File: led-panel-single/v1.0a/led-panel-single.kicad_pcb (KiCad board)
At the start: 2 copper layers, 40 x 20 mm, 23 parts, among them J1 5V, J2 jmp, J3 HUB75E, J4 PMOD, J5 jmp, U1 SN74LVC8T245, U2 NL27WZ14, U3 CD74HC4024PWR, U4 74VHC574

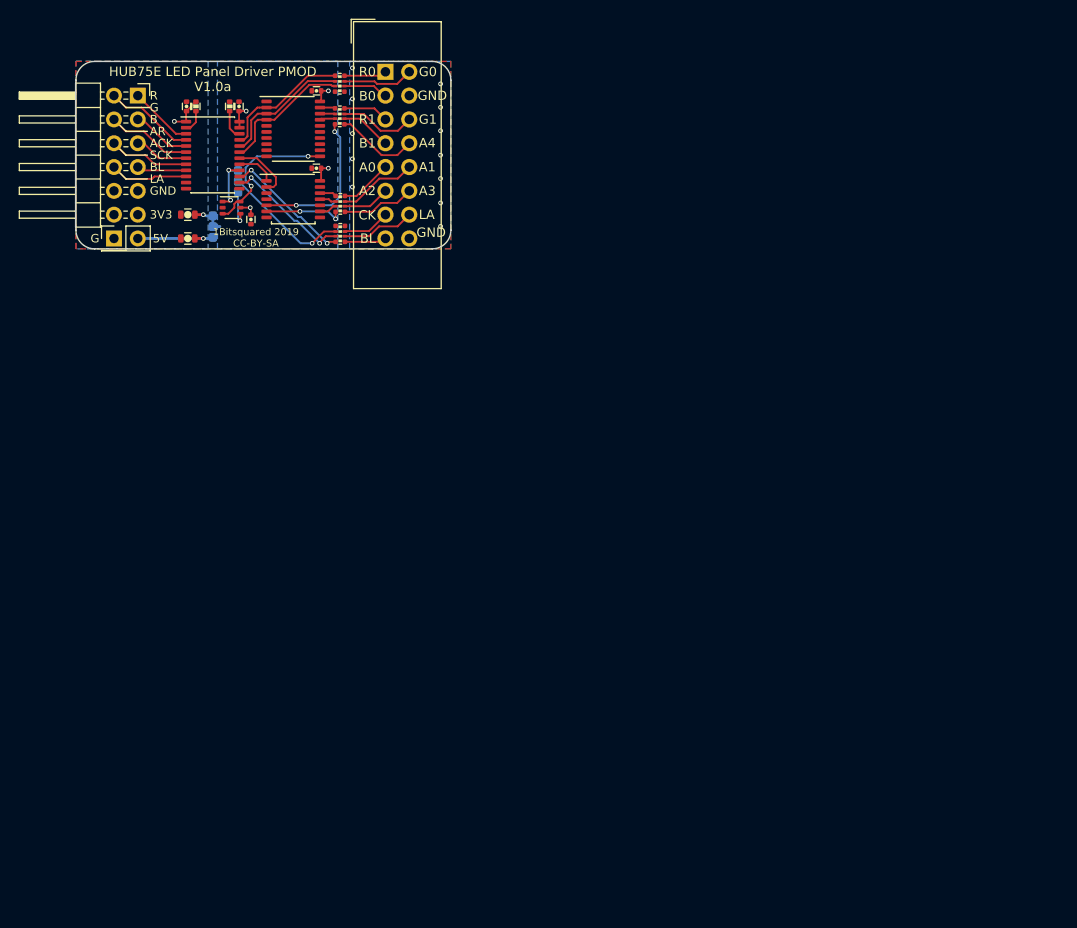
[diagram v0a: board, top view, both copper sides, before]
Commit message: led-panel-single: easy solder version
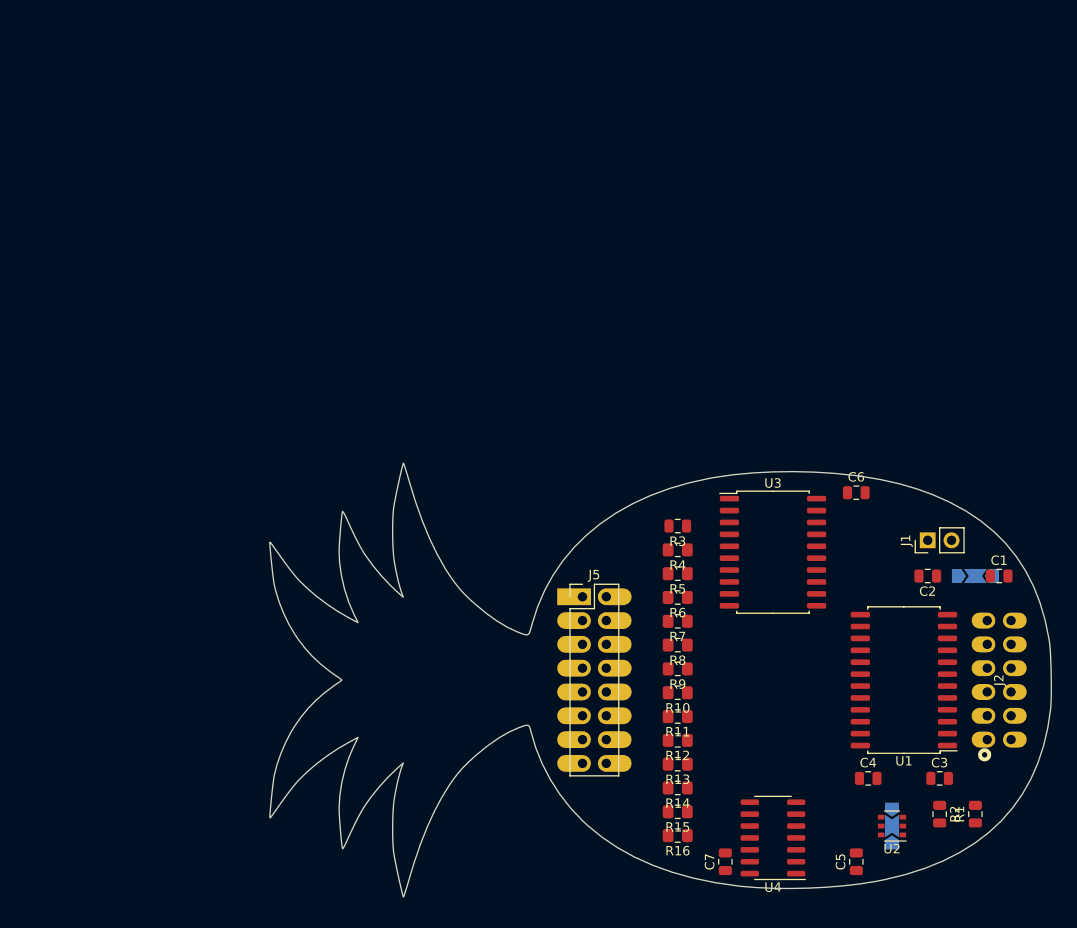
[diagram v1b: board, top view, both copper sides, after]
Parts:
- removed REF**: null_Logo_SilkS_5mm, pkl_logos:null_Logo_SilkS_5mm
- added G***: LOGO, library:pineapple-90, F.Cu at (100.0, 100.0)
- added R10: 33, tom-passives:C_0805_2012Metric_Pad1.15x1.40mm_HandSolder, F.Cu at (101.6, 101.3)
- added R11: 33, tom-passives:C_0805_2012Metric_Pad1.15x1.40mm_HandSolder, F.Cu at (101.6, 103.9)
- added R12: 33, tom-passives:C_0805_2012Metric_Pad1.15x1.40mm_HandSolder, F.Cu at (101.6, 106.4)
- added R13: 33, tom-passives:C_0805_2012Metric_Pad1.15x1.40mm_HandSolder, F.Cu at (101.6, 109.0)
- added R14: 33, tom-passives:C_0805_2012Metric_Pad1.15x1.40mm_HandSolder, F.Cu at (101.6, 111.5)
- added R15: 33, tom-passives:C_0805_2012Metric_Pad1.15x1.40mm_HandSolder, F.Cu at (101.6, 114.0)
- added R16: 33, tom-passives:C_0805_2012Metric_Pad1.15x1.40mm_HandSolder, F.Cu at (101.6, 116.6)
- added R7: 33, tom-passives:C_0805_2012Metric_Pad1.15x1.40mm_HandSolder, F.Cu at (101.6, 93.7)
- added R8: 33, tom-passives:C_0805_2012Metric_Pad1.15x1.40mm_HandSolder, F.Cu at (101.6, 96.3)
- added R9: 33, tom-passives:C_0805_2012Metric_Pad1.15x1.40mm_HandSolder, F.Cu at (101.6, 98.8)
- C1, C2: value 10u -> 10uF,25V,X5R; footprint pkl_dipol:C_0603 -> tom-passives:C_0805_2012Metric
- C3, C4, C5, C6, C7: value 100n -> 100nF,50V,X7R; footprint pkl_dipol:C_0402 -> tom-passives:C_0805_2012Metric
- J1: footprint Connector_PinHeader_2.54mm:PinHeader_2x01_P2.54mm_Vertical -> tom-connectors:PinHeader_1x02_P2.54mm_Vertical
- J2: value jmp -> PMOD; footprint pkl_jumpers:J_NCNO_0903_30 -> tom-connectors:PMOD_2X6_PTH_RA_PLUG; moved to F.Cu
- J3: value HUB75E -> jmp; footprint Connector_IDC:IDC-Header_2x08_P2.54mm_Vertical -> tom-mechanical:SolderJumper-3_P2.0mm_Open_TrianglePad1.0x1.5mm; moved to B.Cu
- J4: value PMOD -> jmp; footprint pkl_connectors:PMODHeader_2x06_P2.54mm_Horizontal -> tom-mechanical:SolderJumper-3_P2.0mm_Open_TrianglePad1.0x1.5mm; moved to B.Cu
- J5: value jmp -> HUB75E; footprint pkl_jumpers:J_NCNO_0903_30 -> tom-connectors:PinHeader_2x08_P2.54mm_Vertical; moved to F.Cu
- R1: footprint pkl_dipol:R_0402 -> tom-passives:R_0805_2012Metric
- R2: value 33E -> 10k; footprint pkl_dipol:R_Array_Convex_4x0402 -> tom-passives:R_0805_2012Metric
- R3: value 10k -> 33; footprint pkl_dipol:R_0402 -> tom-passives:R_0805_2012Metric
- R4, R5, R6: value 33E -> 33; footprint pkl_dipol:R_Array_Convex_4x0402 -> tom-passives:C_0805_2012Metric_Pad1.15x1.40mm_HandSolder
- U1: footprint Package_SO:TSSOP-24_4.4x7.8mm_P0.65mm -> tom-semiconductors:SOIC-24W_7.5x15.4mm_P1.27mm
- U2: footprint Package_TO_SOT_SMD:SOT-363_SC-70-6 -> tom-semiconductors:TSOP-6_1.65x3.05mm_P0.95mm
- U3: value CD74HC4024PWR -> 74VHC574; footprint Package_SO:TSSOP-14_4.4x5mm_P0.65mm -> tom-semiconductors:SOIC-20W_7.5x12.8mm_P1.27mm
- U4: value 74VHC574 -> CD74HC4024PWR; footprint Package_SO:TSSOP-20_4.4x6.5mm_P0.65mm -> tom-semiconductors:SOIC-14_3.9x8.7mm_P1.27mm
- moved R1 112.3 mm to (133.3, 114.3)
- moved C3 107.7 mm to (129.5, 110.5), turned to 0 degrees
- moved C5 104.1 mm to (120.7, 119.4), turned to 90 degrees
- moved J4 103.6 mm to (124.5, 115.6), turned to -90 degrees
- moved J2 97.1 mm to (135.9, 100.0), turned to 90 degrees
- moved U2 96.5 mm to (124.5, 115.6), turned to 180 degrees
- moved C1 94.7 mm to (135.9, 88.9), turned to 0 degrees
- moved J1 92.6 mm to (128.3, 85.1), turned to 90 degrees
- moved U1 92.6 mm to (125.7, 100.0), turned to 180 degrees
- moved U4 91.3 mm to (111.8, 116.8), turned to 180 degrees
- moved R2 91.2 mm to (129.5, 114.3), turned to -90 degrees
- moved C4 88.8 mm to (121.9, 110.5), turned to 0 degrees
- moved C2 86.8 mm to (128.3, 88.9)
- moved C7 85.9 mm to (106.7, 119.4), turned to 90 degrees
- moved J3 82.8 mm to (133.3, 88.9), turned to 180 degrees
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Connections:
- C6 pad 1: GND -> /VCCB
- C6 pad 2: /VCCB -> GND
- C7 pad 1: GND -> /VCCB
- C7 pad 2: /VCCB -> GND
- J2 pad 1: /SCLK -> /iR
- J2 pad 2: /SCLKi -> /iB
- J2 pad 3: /SCLKNN -> /iACLK
- J3 pad 1: /Rx -> +3V3
- J3 pad 2: /Gx -> /VCCB
- J3 pad 3: /Bx -> +5V
- J4 pad 1: /iR -> /SCLK
- J4 pad 2: /iB -> /SCLKi
- J4 pad 3: /iACLK -> /SCLKNN
- J5 pad 1: +3V3 -> /Rx
- J5 pad 2: /VCCB -> /Gx
- J5 pad 3: +5V -> /Bx
- R1 pad 1: Net-(R1-Pad1) -> +3V3
- R1 pad 2: +3V3 -> Net-(U1-Pad2)
- R2 pad 1: /A0 -> Net-(U1-Pad22)
- R2 pad 2: /A0x -> GND
- R3 pad 1: Net-(R3-Pad1) -> /R
- R3 pad 2: GND -> /Rx
- R4 pad 1: (no net) -> /G
- R4 pad 2: (no net) -> /Gx
- R5 pad 1: /R -> /B
- R5 pad 2: /Rx -> /Bx
- U1 pad 2: Net-(R1-Pad1) -> Net-(U1-Pad2)
- U1 pad 22: Net-(R3-Pad1) -> Net-(U1-Pad22)
- U3 pad 1: /ACLK -> GND
- U3 pad 10: (no net) -> GND
- U3 pad 11: /A1 -> /SCLKN
- U3 pad 12: /A0 -> unconnected-(U3-Pad12)
- U3 pad 13: (no net) -> unconnected-(U3-Pad13)
- U3 pad 14: /VCCB -> unconnected-(U3-Pad14)
- U3 pad 2: /ARST -> /R
- U3 pad 3: (no net) -> /G
- U3 pad 4: (no net) -> /B
- U3 pad 5: /A4 -> unconnected-(U3-Pad5)
- U3 pad 6: /A3 -> unconnected-(U3-Pad6)
- U3 pad 7: GND -> unconnected-(U3-Pad7)
- U3 pad 8: (no net) -> unconnected-(U3-Pad8)
- U3 pad 9: /A2 -> unconnected-(U3-Pad9)
- U4 pad 1: GND -> /ACLK
- U4 pad 10: GND -> unconnected-(U4-Pad10)
- U4 pad 11: /SCLKN -> /A1
- U4 pad 12: (no net) -> /A0
- U4 pad 13: (no net) -> unconnected-(U4-Pad13)
- U4 pad 14: (no net) -> /VCCB
- U4 pad 2: /R -> /ARST
- U4 pad 3: /G -> unconnected-(U4-Pad3)
- U4 pad 4: /B -> unconnected-(U4-Pad4)
- U4 pad 5: (no net) -> /A4
- U4 pad 6: (no net) -> /A3
- U4 pad 7: (no net) -> GND
- U4 pad 8: (no net) -> unconnected-(U4-Pad8)
- U4 pad 9: (no net) -> /A2
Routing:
- net /A4: track 16.2 -> 0.00 mm, vias 2 -> 0
- net /SCLKN: track 15.5 -> 0.00 mm, vias 2 -> 0
- net /B: track 14.4 -> 0.00 mm
- net /G: track 14.3 -> 0.00 mm
- net /R: track 14.2 -> 0.00 mm
- net /BLANK: track 13.8 -> 0.00 mm, vias 2 -> 0
- net /LATCH: track 13.8 -> 0.00 mm, vias 2 -> 0
- net /SCLKi: track 13.7 -> 0.00 mm, vias 1 -> 0
- net /iG: track 9.65 -> 0.00 mm
- net /VCCB: track 9.31 -> 0.00 mm, vias 4 -> 0
- net /iARST: track 9.13 -> 0.00 mm
- net +5V: track 8.96 -> 0.00 mm, vias 1 -> 0
- net /A4x: track 8.80 -> 0.00 mm
- net /iSCLK: track 8.62 -> 0.00 mm
- net /A3: track 8.53 -> 0.00 mm, vias 2 -> 0
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- removed copper zone on B.Cu, net +3V3
- removed copper zone on B.Cu, net /VCCB
- removed copper zone on B.Cu, net GND
- removed copper zone on F.Cu, net GND
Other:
- board size 40 x 20 mm -> 83.4 x 46.3 mm
- net class Default removed
- rule pad_to_mask_clearance: 0.05 -> 0
- board text removed: "1Bitsquared 2019 CC-BY-SA"
- board text removed: "3V3"
- board text removed: "5V"
- board text removed: "A0"
- board text removed: "A1"
- board text removed: "A2"
- board text removed: "A3"
- board text removed: "A4"
- board text removed: "ACK"
- board text removed: "AR"
- board text removed: "B"
- board text removed: "B0"
- board text removed: "B1"
- board text removed: "BL"
- board text removed: "CK"
- board text removed: "Color Data Clock Select"
- board text removed: "G"
- board text removed: "G0"
- board text removed: "G1"
- board text removed: "GND"
- board text removed: "HUB75E LED Panel Driver PMOD V1.0a"
- board text removed: "LA"
- board text removed: "NULL"
- board text removed: "Output IO Voltage Select"
- board text removed: "R"
- board text removed: "R0"
- board text removed: "R1"
- board text removed: "SCK"
- board text removed: "SCKNN"
- board text removed: "V1.0a HUB75E LED Panel Driver PMOD"

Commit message: led-panel-single: Jan 2023 edition
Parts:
- removed J1: 5V, tom-connectors:PinHeader_1x02_P2.54mm_Vertical
- added D1: LED, tom-opto:LED_0805_2012Metric_Pad1.15x1.40mm_HandSolder, F.Cu at (135.1, 85.9)
- added G***: LOGO, library:pineapple-silk, B.Cu at (100.0, 100.0)
- added R3: 1k, tom-passives:R_0805_2012Metric, F.Cu at (127.3, 81.5)
- moved C5 36.9 mm to (120.7, 82.5), turned to 180 degrees
- moved J4 29.3 mm to (122.0, 86.4)
- moved U2 29.3 mm to (122.0, 86.4)
- moved R2 5.71 mm to (123.8, 114.3)
- moved C3 0.67 mm to (130.2, 110.5), turned to 90 degrees
- moved C7 0.63 mm to (106.7, 118.7), turned to -90 degrees
- renumbered R9 to R10, R10 to R11, R11 to R12, R12 to R13, R13 to R14, R14 to R15, R15 to R16, R16 to R17, R3 to R4, R4 to R5, R5 to R6, R6 to R7, R7 to R8, R8 to R9
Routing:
- net /VCCB: track 0.00 -> 101.2 mm, vias 0 -> 6
- net /SCLKi: track 0.00 -> 66.0 mm, vias 0 -> 3
- net /LATCH: track 0.00 -> 59.2 mm, vias 0 -> 2
- net /BLANK: track 0.00 -> 54.5 mm, vias 0 -> 2
- net +3V3: track 0.00 -> 51.7 mm, vias 0 -> 2
- net /A0x: track 0.00 -> 44.6 mm
- net /ACLK: track 0.00 -> 37.9 mm
- net /R: track 0.00 -> 36.4 mm, vias 0 -> 2
- net /ARST: track 0.00 -> 34.5 mm
- net /G: track 0.00 -> 33.5 mm, vias 0 -> 2
- net /B1x: track 0.00 -> 33.3 mm, vias 0 -> 1
- net /B: track 0.00 -> 31.7 mm
- net /B1: track 0.00 -> 30.2 mm, vias 0 -> 2
- net /A4: track 0.00 -> 28.8 mm
- net /A0: track 0.00 -> 28.7 mm
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- added copper zone on B.Cu, net GND
- added copper zone on F.Cu, net GND
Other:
- board text added: "+"
- board text added: "G"
- board text added: "HUB75 PMOD SINGLE @TomKeddie Jan 2023"
- board text added: "o"
